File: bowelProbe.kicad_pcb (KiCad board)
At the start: 4 copper layers, 72.5 x 40.1 mm, 105 parts, among them J1 Conn_01x01, J12 Conn_01x01, J13 Conn_01x01, J14 Conn_01x01, J15 Conn_01x01, J16 Conn_01x01, J17 Conn_01x01, J18 Conn_01x01, J19 Conn_01x01, J2 Conn_01x01, J20 Conn_01x01, J21 Conn_01x01, J3 Conn_01x08, J4 Conn_01x08, U10 TLV76050DBZR, U11 TL072ACDR, U2 LT8330, U3 ATmega328P, U4 AD9833BRMZ, U6 OPA2134UA/2K5, U7 TL072ACDR, U8 MCP6002T-E/MC, U9 LM3480IM3-12/NOPB

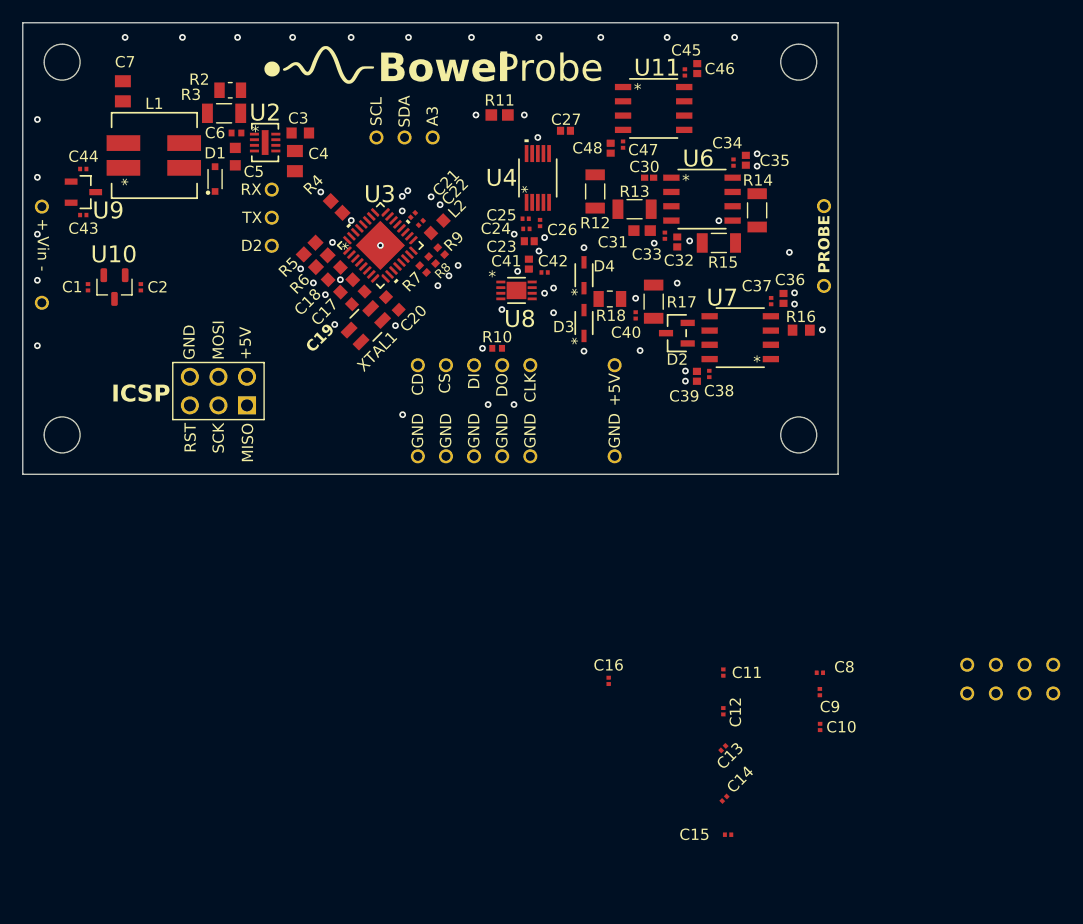
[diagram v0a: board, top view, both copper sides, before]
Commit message: Schematic/Layout
Finished checking schematic, all looks good. Added remaining parts from schematic into layout (including test nodes). Next step is to plan layout for rough draft.
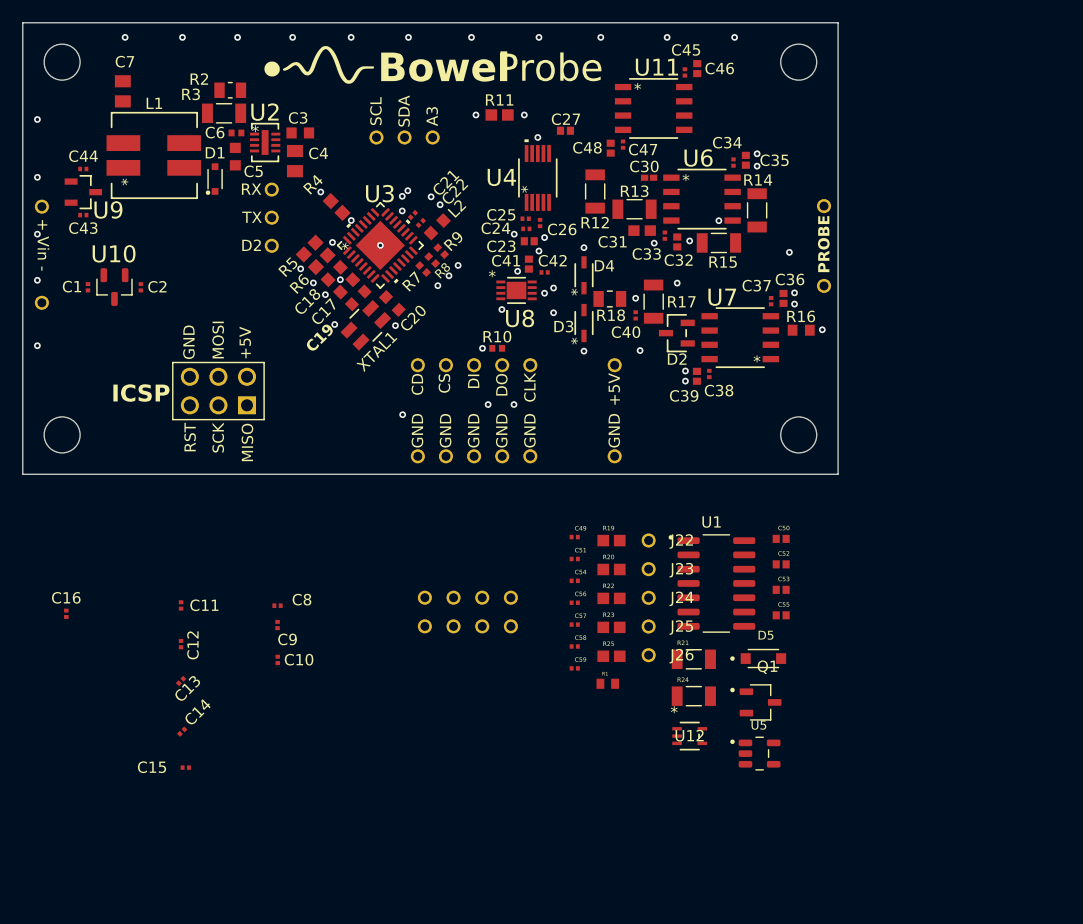
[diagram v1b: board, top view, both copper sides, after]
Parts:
- added C49: 0.1u, BowelProbe:Cap0.1uF, F.Cu at (110.3, 91.3)
- added C50: 10u, BowelProbe:Cap10uF, F.Cu at (128.6, 91.5)
- added C51: 0.1u, BowelProbe:Cap0.1uF, F.Cu at (110.3, 93.3)
- added C52: 10u, BowelProbe:Cap10uF, F.Cu at (128.6, 93.8)
- added C53: 10u, BowelProbe:Cap10uF, F.Cu at (128.6, 96.0)
- added C54: 0.1u, BowelProbe:Cap0.1uF, F.Cu at (110.3, 95.2)
- added C55: 10u, BowelProbe:Cap10uF, F.Cu at (128.6, 98.3)
- added C56: 0.1u, BowelProbe:Cap0.1uF, F.Cu at (110.3, 97.2)
- added C57: 0.1u, BowelProbe:Cap0.1uF, F.Cu at (110.3, 99.1)
- added C58: 0.1u, BowelProbe:Cap0.1uF, F.Cu at (110.3, 101.1)
- added C59: 0.1u, BowelProbe:Cap0.1uF, F.Cu at (110.3, 103.0)
- added D5: BZT52B12, BowelProbe:BZT52B12, F.Cu at (127.1, 102.1)
- added J22: Conn_01x01, BowelProbe:CT3149-2, F.Cu at (116.9, 91.6)
- added J23: Conn_01x01, BowelProbe:CT3149-2, F.Cu at (116.9, 94.2)
- added J24: Conn_01x01, BowelProbe:CT3149-2, F.Cu at (116.9, 96.7)
- added J25: Conn_01x01, BowelProbe:CT3149-2, F.Cu at (116.9, 99.3)
- added J26: Conn_01x01, BowelProbe:CT3149-2, F.Cu at (116.9, 101.8)
- added Q1: AO3407A, BowelProbe:AO3407A, F.Cu at (126.8, 106.0)
- added R1: 100k, BowelProbe:Resistor100k, F.Cu at (113.2, 104.4)
- added R19: 10k, BowelProbe:Resistor10k, F.Cu at (113.6, 91.6)
- added R20: 10k, BowelProbe:Resistor10k, F.Cu at (113.6, 94.2)
- added R21: 30k, BowelProbe:Resistor30k, F.Cu at (120.9, 102.2)
- added R22: 10k, BowelProbe:Resistor10k, F.Cu at (113.6, 96.8)
- added R23: 10k, BowelProbe:Resistor10k, F.Cu at (113.6, 99.4)
- added R24: 30k, BowelProbe:Resistor30k, F.Cu at (120.9, 105.5)
- added R25: 10k, BowelProbe:Resistor10k, F.Cu at (113.6, 101.9)
- added U1: LM319MX/NOPB, BowelProbe:LM319MX_NOPB, F.Cu at (122.9, 95.5)
- added U12: Buffer, BowelProbe:Buffer, F.Cu at (120.5, 109.0)
- added U5: SN74LVC1G86DBVR, BowelProbe:SN74LVC1G86DBVR, F.Cu at (126.7, 110.6)
- moved C14 48.6 mm to (75.4, 108.6)
- moved J18 48.6 mm to (102.1, 96.7)
- moved J19 48.6 mm to (102.1, 99.3)
- moved C10 48.6 mm to (83.9, 102.3)
- moved C11 48.6 mm to (75.3, 97.4)
- moved C12 48.6 mm to (75.3, 100.9)
- moved C13 48.6 mm to (75.3, 104.1)
- moved C15 48.6 mm to (75.7, 111.8)
- moved C16 48.6 mm to (65.1, 98.2)
- moved C8 48.6 mm to (83.9, 97.4)
- moved C9 48.6 mm to (83.9, 99.2)
- moved J14 48.6 mm to (97.0, 96.7)
- moved J15 48.6 mm to (97.0, 99.3)
- moved J16 48.6 mm to (99.5, 96.7)
- moved J17 48.6 mm to (99.5, 99.3)
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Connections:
- C1 pad 1: /Vin -> Net-(J26-Pin_1)
- C43 pad 1: /Vin -> Net-(J26-Pin_1)
- U10 pad 2: /Vin -> Net-(J26-Pin_1)
- U3 pad 19: /A6 -> /PDoutBuf
- U9 pad 2: /Vin -> Net-(J26-Pin_1)

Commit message: Layout Update
Schematic rechecked and passed check #2. Initial rough draft layout nearly complete; just need to add stitching capacitors. Silkscreen text sizes and thicknesses changed.
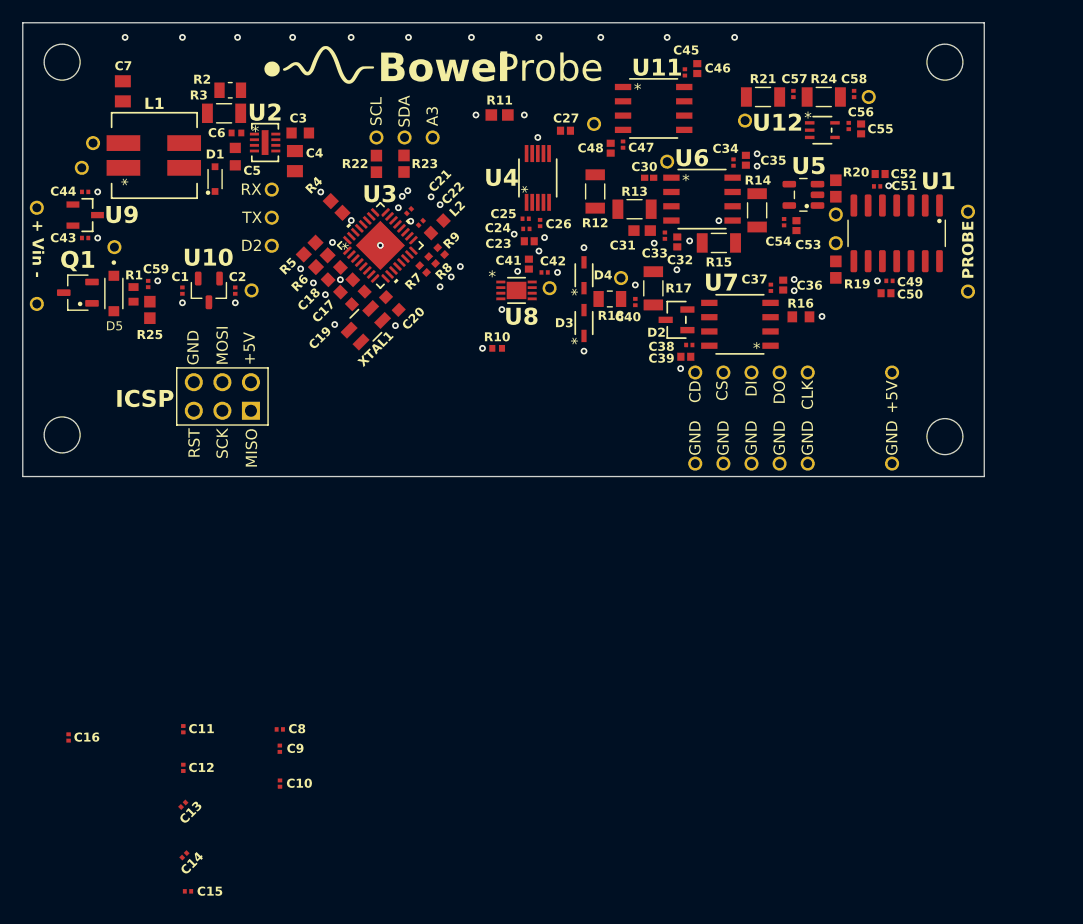
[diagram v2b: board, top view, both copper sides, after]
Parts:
- removed J19: Conn_01x01, BowelProbe:CT3149-2
- moved Q1 70.8 mm to (66.1, 69.6), turned to 180 degrees
- moved D5 66.3 mm to (69.3, 69.7), turned to -90 degrees
- moved J26 59.8 mm to (69.3, 65.5)
- moved U12 55.2 mm to (132.3, 55.1)
- moved C58 55.1 mm to (135.1, 51.9), turned to -90 degrees
- moved R1 54.6 mm to (71.0, 69.8), turned to 90 degrees
- moved R24 54.5 mm to (132.4, 52.2)
- moved J16 51.6 mm to (67.5, 56.3)
- moved R25 51.3 mm to (72.5, 71.1), turned to 90 degrees
- moved C59 51.1 mm to (72.3, 68.8), turned to 90 degrees
- moved C57 51.0 mm to (129.7, 51.9), turned to -90 degrees
- moved J25 51.0 mm to (136.4, 52.2)
- moved R21 50.4 mm to (127.0, 52.2)
- moved U5 49.8 mm to (130.6, 60.9), turned to 180 degrees
- moved J14 48.9 mm to (66.5, 58.5)
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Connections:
- net /Vbuffer renamed Net-(U7-1IN-)
- net Net-(J26-Pin_1) renamed /VinReverse
- U3 pad 13: unconnected-(U3-PB1-Pad13) -> /D9
- U3 pad 14: unconnected-(U3-PB2-Pad14) -> /D10
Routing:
- net GND: vias 39 -> 37
- net /VADC: vias 2 -> 1
- net /PDoutBuf: vias 0 -> 1
- net /+5V: vias 11 -> 9
- net /+12V: vias 2 -> 1
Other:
- board size 72.5 x 40.1 mm -> 85.5 x 40.4 mm

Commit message: Layout Rough Draft Done
Placed all components where needed. Exposed remaining I/O pins on ATMega for miscellaneous use. Expected vias and stitching caps added. More stitching caps and vias will be added as necessary throughout and after routing. Considering possibility of moving logo and extra pin placements. Layout review coming up soon.
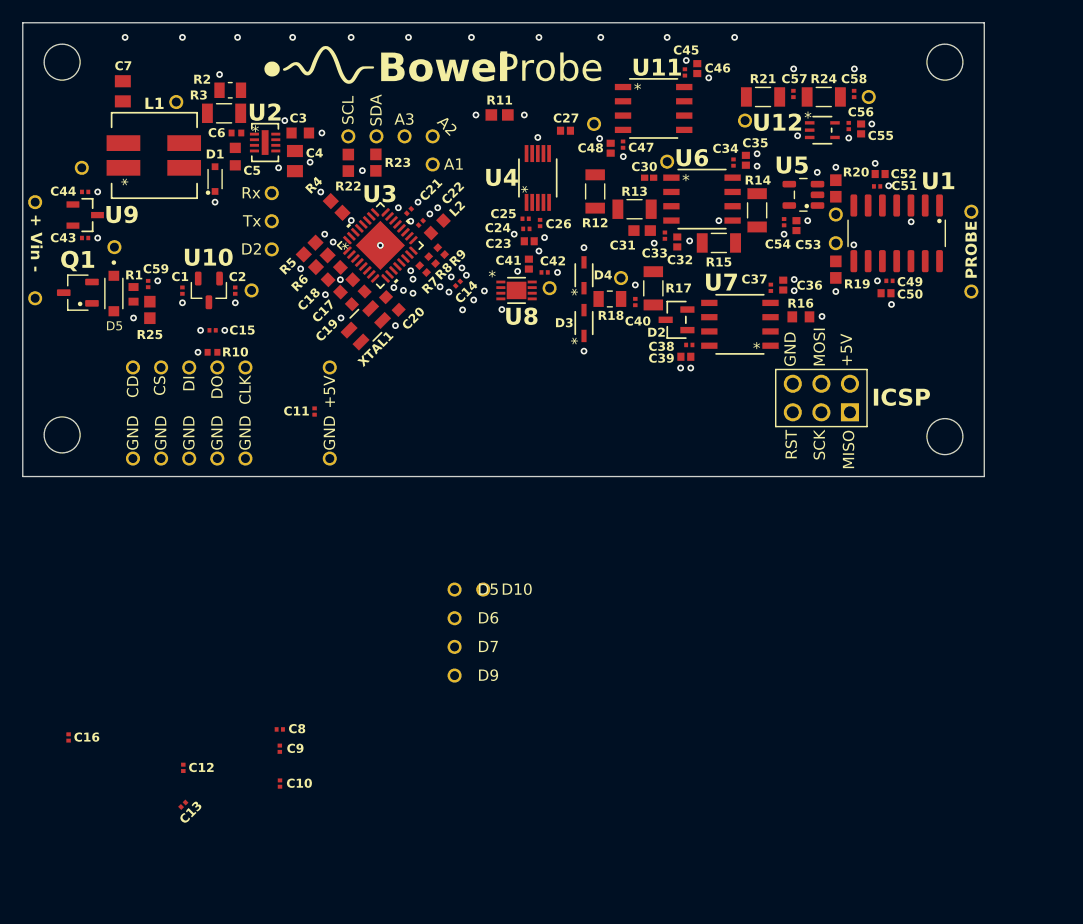
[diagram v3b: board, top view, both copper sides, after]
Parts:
- added A1: Conn_01x01, BowelProbe:CT3149-0, F.Cu at (97.7, 58.2)
- added A2: Conn_01x01, BowelProbe:CT3149-0, F.Cu at (97.7, 55.7)
- added D10: Conn_01x01, BowelProbe:CT3149-0, F.Cu at (102.2, 96.0)
- added D5: Conn_01x01, BowelProbe:CT3149-0, F.Cu at (99.6, 96.0)
- added D6: Conn_01x01, BowelProbe:CT3149-0, F.Cu at (99.6, 98.5)
- added D7: Conn_01x01, BowelProbe:CT3149-0, F.Cu at (99.6, 101.1)
- added D9: Conn_01x01, BowelProbe:CT3149-0, F.Cu at (99.6, 103.7)
- moved C14 56.4 mm to (99.9, 68.8)
- moved ICSP 53.3 mm to (132.2, 79.0)
- moved J3 50.0 mm to (79.8, 76.2)
- moved J4 50.0 mm to (79.8, 84.3)
- moved C15 49.9 mm to (78.1, 73.0)
- moved C11 30.6 mm to (87.2, 80.2)
- moved R10 25.3 mm to (78.1, 74.9)
- moved J16 8.25 mm to (74.8, 52.6)
- moved R22 2.50 mm to (90.2, 58.0)
- moved R23 2.50 mm to (92.6, 58.0)
- moved A3 2.50 mm to (95.2, 55.7)
- moved SCL 2.50 mm to (90.2, 55.7)
- moved SDA 2.50 mm to (92.7, 55.7)
- moved J1 0.52 mm to (62.3, 70.1)
- moved J2 0.52 mm to (62.3, 61.5)
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- renumbered RX to Rx, TX to Tx
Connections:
- U3 pad 23: /A0 -> /nSS_Sin
- U3 pad 25: /nSS_Sin -> /A2
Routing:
- net GND: vias 37 -> 54
- net /SCK: vias 1 -> 2
- net /MOSI: vias 1 -> 2
- net /MISO: vias 2 -> 3
- net /D9: vias 0 -> 1
- net /D7: vias 0 -> 1
- net /D6: vias 0 -> 1
- net /D5: vias 0 -> 1
- net /D10: vias 0 -> 1
- net /-12V: vias 2 -> 3
- net /+5V: vias 9 -> 15
- net /+12V: vias 1 -> 6
